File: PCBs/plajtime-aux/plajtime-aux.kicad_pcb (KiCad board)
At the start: 2 copper layers, 50.7 x 23.5 mm, 21 parts, among them J1 Slider, J2 USB, J3 Internal connector, J4 LRA, U1 USBLC6-2P6, U2 IQS7222B, U3 DA7280

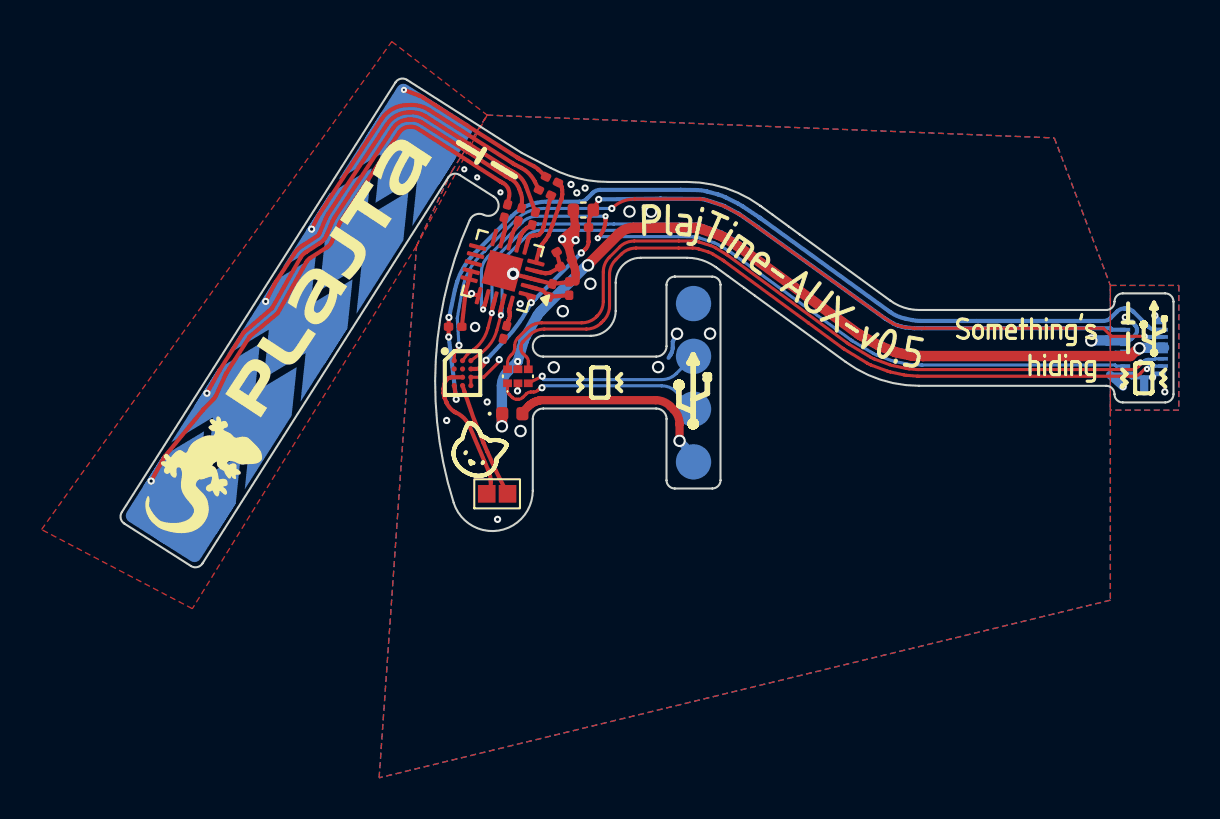
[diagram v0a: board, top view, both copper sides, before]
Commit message: Edited via sizes
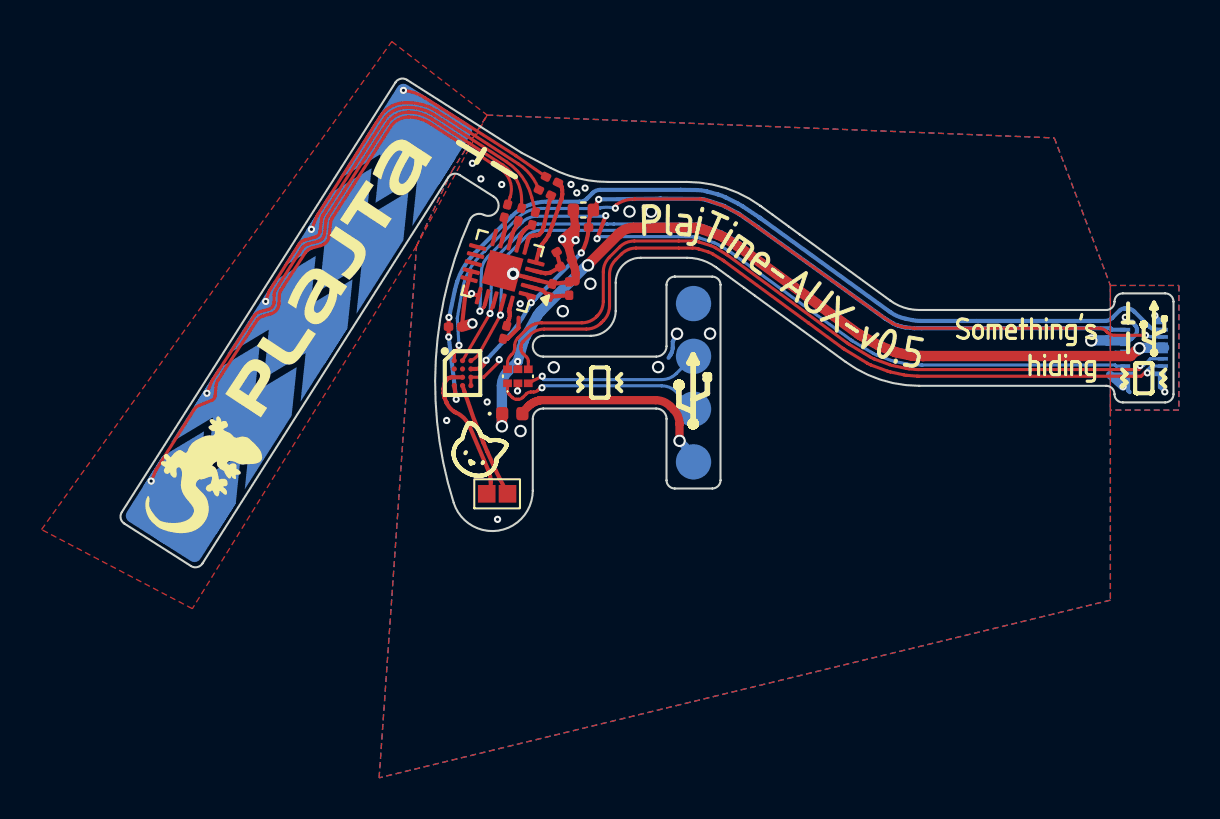
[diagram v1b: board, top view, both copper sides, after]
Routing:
- net GND: track 22.5 -> 24.1 mm, vias 32 -> 31
- net Net-(J1-Pin_5): track 27.8 -> 29.3 mm
- net Net-(J1-Pin_4): track 24.0 -> 24.9 mm
- net Net-(J1-Pin_3): track 19.8 -> 20.4 mm
